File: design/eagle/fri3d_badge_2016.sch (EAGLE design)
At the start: 43 parts, among them K1 65100516121, Q1 MOSFET-NCHANNEL2N7002PW, U1 MCP73831

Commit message: fixed RGB LED footprint (+draft silk)
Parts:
- removed D2: (no value), SparkFun-LED:0.13_RGB_LEDPLCC
- added U$4: DRAGAN-PERSONAL_AVAGO-RGB-LED, Badge_EZR_V1:DRAGAN-PERSONAL_AVAGO-RGB-LED
- LED1: value (none) -> IR LED 1
- LED2: value (none) -> IR LED 2
- LED3: value (none) -> IR LED 3
- LED4: value (none) -> IR LED 4
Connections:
- removed net N$21: D2.RED, R9.2
- new net N$18: R9.2, U$4.P$4
- net N$19: now also R8.2, U$4.P$3; no longer D2.BLUE, R7.2
- net N$20: now also R7.2, U$4.P$2; no longer D2.GREEN, R8.2
- net VCC: now also U$4.P$1; no longer D2.ANODE
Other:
- moved on the sheet: R16, R17, R7, R8, R9
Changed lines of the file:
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@@
 <part name="GND8" library="SparkFun-Aesthetics" deviceset="GND" device=""/>
 <part name="S1" library="SparkFun-Electromechanical" deviceset="SWITCH-MOMENTARY-2" device="PTH"/>
-<part name="D2" library="SparkFun-LED" deviceset="0.13_RGB_LED" device="PLCC"/>
 <part name="ICSP" library="SparkFun-Connectors" deviceset="PINHD-2X3" device=""/>
 <part name="GND9" library="SparkFun-Aesthetics" deviceset="GND" device=""/>
@@
 <part name="R16" library="SparkFun-Passives" deviceset="RESISTOR" device="0805-RES" value="220"/>
 <part name="R17" library="SparkFun-Passives" deviceset="RESISTOR" device="0805-RES" value="220"/>
-<part name="LED1" library="led" deviceset="LED" device="CHIPLED_0805"/>
-<part name="LED2" library="led" deviceset="LED" device="CHIPLED_0805"/>
-<part name="LED3" library="led" deviceset="LED" device="CHIPLED_0805"/>
-<part name="LED4" library="led" deviceset="LED" device="CHIPLED_0805"/>
+<part name="LED1" library="led" deviceset="LED" device="CHIPLED_0805" value="IR LED 1"/>
+<part name="LED2" library="led" deviceset="LED" device="CHIPLED_0805" value="IR LED 2"/>
+<part name="LED3" library="led" deviceset="LED" device="CHIPLED_0805" value="IR LED 3"/>
+<part name="LED4" library="led" deviceset="LED" device="CHIPLED_0805" value="IR LED 4"/>
 <part name="Q2" library="crystal" deviceset="CRYSTAL" device="HC49S"/>
 <part name="J3" library="SparkFun-Connectors" deviceset="M02" device="JST-PTH-VERT"/>
@@
 <part name="GND10" library="SparkFun-Aesthetics" deviceset="GND" device=""/>
 <part name="S2" library="SparkFun-Electromechanical" deviceset="SWITCH-SPDT" device="-SMD-A"/>
+<part name="U$4" library="Badge_EZR_V1" deviceset="DRAGAN-PERSONAL_AVAGO-RGB-LED" device=""/>
 </parts>
 <sheets>
@@
 <instance part="GND8" gate="1" x="45.72" y="96.52" rot="R270"/>
 <instance part="S1" gate="G$1" x="185.42" y="160.02" rot="R180"/>
-<instance part="D2" gate="G$1" x="198.12" y="116.84" rot="R270"/>
 <instance part="ICSP" gate="A" x="-17.78" y="35.56"/>
 <instance part="GND9" gate="1" x="152.4" y="60.96"/>
 <instance part="SUPPLY4" gate="G$1" x="213.36" y="73.66"/>
 <instance part="SUPPLY5" gate="G$1" x="215.9" y="160.02"/>
-<instance part="R7" gate="G$1" x="182.88" y="124.46"/>
-<instance part="R8" gate="G$1" x="182.88" y="116.84"/>
-<instance part="SUPPLY6" gate="G$1" x="208.28" y="129.54"/>
+<instance part="R7" gate="G$1" x="182.88" y="104.14"/>
+<instance part="R8" gate="G$1" x="182.88" y="114.3"/>
+<instance part="SUPPLY6" gate="G$1" x="220.98" y="127"/>
 <instance part="GND17" gate="1" x="104.14" y="20.32"/>
 <instance part="U$3" gate="G$1" x="71.12" y="27.94"/>
@@
 <instance part="R6" gate="G$1" x="86.36" y="33.02"/>
 <instance part="R11" gate="G$1" x="86.36" y="43.18"/>
-<instance part="R9" gate="G$1" x="187.96" y="104.14" rot="R90"/>
-<instance part="R16" gate="G$1" x="182.88" y="99.06"/>
-<instance part="R17" gate="G$1" x="177.8" y="104.14" rot="R270"/>
+<instance part="R9" gate="G$1" x="187.96" y="129.54" rot="R270"/>
+<instance part="R16" gate="G$1" x="182.88" y="134.62"/>
+<instance part="R17" gate="G$1" x="177.8" y="129.54" rot="R90"/>
 <instance part="LED1" gate="G$1" x="205.74" y="71.12" rot="R270"/>
 <instance part="LED2" gate="G$1" x="205.74" y="55.88" rot="R270"/>
@@
 <instance part="GND10" gate="1" x="167.64" y="139.7"/>
 <instance part="S2" gate="1" x="-7.62" y="66.04"/>
+<instance part="U$4" gate="G$1" x="213.36" y="114.3" rot="R180"/>
 </instances>
 <busses>
@@
 </segment>
 <segment>
-<pinref part="D2" gate="G$1" pin="ANODE"/>
-<pinref part="SUPPLY6" gate="G$1" pin="VCC"/>
-<wire x1="208.28" y1="129.54" x2="208.28" y2="121.92" width="0.1524" layer="91"/>
-<wire x1="208.28" y1="121.92" x2="203.2" y2="121.92" width="0.1524" layer="91"/>
-</segment>
-<segment>
 <pinref part="SUPPLY7" gate="G$1" pin="VCC"/>
 <wire x1="104.14" y1="33.02" x2="99.06" y2="33.02" width="0.1524" layer="91"/>
@@
 <pinref part="S2" gate="1" pin="S"/>
 <wire x1="-2.54" y1="63.5" x2="7.62" y2="63.5" width="0.1524" layer="91"/>
+</segment>
+<segment>
+<pinref part="U$4" gate="G$1" pin="P$1"/>
+<pinref part="SUPPLY6" gate="G$1" pin="VCC"/>
+<wire x1="218.44" y1="114.3" x2="220.98" y2="114.3" width="0.1524" layer="91"/>
+<wire x1="220.98" y1="114.3" x2="220.98" y2="127" width="0.1524" layer="91"/>
 </segment>
 </net>
@@
 </segment>
 </net>
-<net name="N$19" class="0">
-<segment>
-<pinref part="R7" gate="G$1" pin="2"/>
-<pinref part="D2" gate="G$1" pin="BLUE"/>
-<wire x1="187.96" y1="124.46" x2="187.96" y2="121.92" width="0.1524" layer="91"/>
-<wire x1="187.96" y1="121.92" x2="195.58" y2="121.92" width="0.1524" layer="91"/>
-</segment>
-</net>
-<net name="N$21" class="0">
-<segment>
-<pinref part="D2" gate="G$1" pin="RED"/>
-<wire x1="187.96" y1="111.76" x2="195.58" y2="111.76" width="0.1524" layer="91"/>
-<pinref part="R9" gate="G$1" pin="2"/>
-<wire x1="187.96" y1="109.22" x2="187.96" y2="111.76" width="0.1524" layer="91"/>
-</segment>
-</net>
 <net name="RGB_BLUE" class="0">
 <segment>
 <pinref part="R7" gate="G$1" pin="1"/>
-<wire x1="177.8" y1="124.46" x2="160.02" y2="124.46" width="0.1524" layer="91"/>
-<label x="160.02" y="124.46" size="1.778" layer="95"/>
+<wire x1="177.8" y1="104.14" x2="160.02" y2="104.14" width="0.1524" layer="91"/>
+<label x="160.02" y="104.14" size="1.778" layer="95"/>
 </segment>
 <segment>
@@
 <segment>
 <pinref part="R8" gate="G$1" pin="1"/>
-<wire x1="177.8" y1="116.84" x2="160.02" y2="116.84" width="0.1524" layer="91"/>
-<label x="160.02" y="116.84" size="1.778" layer="95"/>
+<wire x1="177.8" y1="114.3" x2="160.02" y2="114.3" width="0.1524" layer="91"/>
+<label x="160.02" y="114.3" size="1.778" layer="95"/>
 </segment>
 <segment>
@@
 <net name="RGB_RED" class="0">
 <segment>
-<wire x1="177.8" y1="109.22" x2="160.02" y2="109.22" width="0.1524" layer="91"/>
-<label x="160.02" y="109.22" size="1.778" layer="95"/>
+<wire x1="177.8" y1="124.46" x2="160.02" y2="124.46" width="0.1524" layer="91"/>
+<label x="160.02" y="124.46" size="1.778" layer="95"/>
 <pinref part="R17" gate="G$1" pin="1"/>
 </segment>
@@
 <wire x1="106.68" y1="109.22" x2="142.24" y2="109.22" width="0.1524" layer="91"/>
 <label x="132.08" y="109.22" size="1.778" layer="95"/>
-</segment>
-</net>
-<net name="N$20" class="0">
-<segment>
-<pinref part="R8" gate="G$1" pin="2"/>
-<pinref part="D2" gate="G$1" pin="GREEN"/>
-<wire x1="187.96" y1="116.84" x2="195.58" y2="116.84" width="0.1524" layer="91"/>
 </segment>
 </net>
@@
 </segment>
 </net>
+<net name="N$19" class="0">
+<segment>
+<pinref part="R8" gate="G$1" pin="2"/>
+<pinref part="U$4" gate="G$1" pin="P$3"/>
+<wire x1="187.96" y1="114.3" x2="193.04" y2="114.3" width="0.1524" layer="91"/>
+</segment>
+</net>
+<net name="N$18" class="0">
+<segment>
+<pinref part="R9" gate="G$1" pin="2"/>
+<pinref part="U$4" gate="G$1" pin="P$4"/>
+<wire x1="187.96" y1="124.46" x2="193.04" y2="124.46" width="0.1524" layer="91"/>
+</segment>
+</net>
+<net name="N$20" class="0">
+<segment>
+<pinref part="R7" gate="G$1" pin="2"/>
+<pinref part="U$4" gate="G$1" pin="P$2"/>
+<wire x1="187.96" y1="104.14" x2="193.04" y2="104.14" width="0.1524" layer="91"/>
+</segment>
+</net>

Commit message: fixed USB connector (Mouser)
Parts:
- removed K1: 65100516121, Input-Output_Connectors_rev15d:65100516121
- added U$5: OCTA-CORE_MCIRO-USB2MOUSER, OCTA-EZR_v1:OCTA-CORE_MCIRO-USB2MOUSER
- LED5: value (none) -> LED
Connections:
- net GND: now also U$5.P$5, U$5.P$6, U$5.P$7; no longer K1.5GND, K1.GND@1, K1.GND@2
- net N$1: now also U$5.P$2; no longer K1.2D-
- net N$2: now also U$5.P$3; no longer K1.3D+
- net USBVCC: now also U$5.P$1; no longer K1.1VCC
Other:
- moved on the sheet: R1, R2
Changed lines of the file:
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@@
 <part name="SUPPLY8" library="SparkFun-Aesthetics" deviceset="VCC" device=""/>
 <part name="GND18" library="SparkFun-Aesthetics" deviceset="GND" device=""/>
-<part name="LED5" library="adafruit" deviceset="LED" device="CHIPLED_0805"/>
+<part name="LED5" library="adafruit" deviceset="LED" device="CHIPLED_0805" value="LED"/>
 <part name="R10" library="SparkFun-Passives" deviceset="RESISTOR" device="0805-RES" value="220"/>
 <part name="C7" library="SparkFun-Capacitors" deviceset="CAP" device="0805" value="0.1uF"/>
@@
 <part name="Q2" library="crystal" deviceset="CRYSTAL" device="HC49S"/>
 <part name="J3" library="SparkFun-Connectors" deviceset="M02" device="JST-PTH-VERT"/>
-<part name="K1" library="Input-Output_Connectors_rev15d" deviceset="65100516121" device=""/>
 <part name="U$2" library="GeekAmmo" deviceset="HEADER-06X1?" device="-MALE"/>
 <part name="R18" library="SparkFun-Passives" deviceset="RESISTOR" device="0805-RES" value="10K"/>
@@
 <part name="S2" library="SparkFun-Electromechanical" deviceset="SWITCH-SPDT" device="-SMD-A"/>
 <part name="U$4" library="Badge_EZR_V1" deviceset="DRAGAN-PERSONAL_AVAGO-RGB-LED" device=""/>
+<part name="U$5" library="OCTA-EZR_v1" deviceset="OCTA-CORE_MCIRO-USB2" device="" technology="MOUSER"/>
 </parts>
 <sheets>
@@
 <instance part="FRAME2" gate="G$1" x="-45.72" y="-7.62"/>
 <instance part="U$1" gate="G$1" x="88.9" y="109.22"/>
-<instance part="R1" gate="G$1" x="7.62" y="139.7"/>
-<instance part="R2" gate="G$1" x="7.62" y="132.08"/>
+<instance part="R1" gate="G$1" x="7.62" y="137.16"/>
+<instance part="R2" gate="G$1" x="7.62" y="129.54"/>
 <instance part="GND1" gate="1" x="-7.62" y="142.24"/>
 <instance part="U1" gate="G$1" x="0" y="96.52"/>
@@
 <instance part="Q2" gate="G$1" x="63.5" y="96.52" rot="R90"/>
 <instance part="J3" gate="G$1" x="-30.48" y="63.5"/>
-<instance part="K1" gate="G$1" x="-22.86" y="134.62" rot="R180"/>
 <instance part="U$2" gate="G$1" x="20.32" y="35.56"/>
 <instance part="R18" gate="G$1" x="167.64" y="147.32" rot="R270"/>
@@
 <instance part="S2" gate="1" x="-7.62" y="66.04"/>
 <instance part="U$4" gate="G$1" x="213.36" y="114.3" rot="R180"/>
+<instance part="U$5" gate="G$1" x="-25.4" y="137.16" rot="R180"/>
 </instances>
 <busses>
@@
 </segment>
 <segment>
-<pinref part="K1" gate="G$1" pin="5GND"/>
-<wire x1="-15.24" y1="139.7" x2="-15.24" y2="144.78" width="0.1524" layer="91"/>
 <wire x1="-15.24" y1="144.78" x2="-15.24" y2="147.32" width="0.1524" layer="91"/>
 <wire x1="-15.24" y1="147.32" x2="-7.62" y2="147.32" width="0.1524" layer="91"/>
 <pinref part="GND1" gate="1" pin="GND"/>
 <wire x1="-7.62" y1="147.32" x2="-7.62" y2="144.78" width="0.1524" layer="91"/>
-<pinref part="K1" gate="G$1" pin="GND@1"/>
-<wire x1="-17.78" y1="144.78" x2="-15.24" y2="144.78" width="0.1524" layer="91"/>
+<junction x="-15.24" y="147.32"/>
+<pinref part="U$5" gate="G$1" pin="P$7"/>
+<wire x1="-22.86" y1="147.32" x2="-15.24" y2="147.32" width="0.1524" layer="91"/>
+<pinref part="U$5" gate="G$1" pin="P$6"/>
+<wire x1="-22.86" y1="144.78" x2="-15.24" y2="144.78" width="0.1524" layer="91"/>
+<pinref part="U$5" gate="G$1" pin="P$5"/>
+<wire x1="-20.32" y1="134.62" x2="-15.24" y2="134.62" width="0.1524" layer="91"/>
+<wire x1="-15.24" y1="134.62" x2="-15.24" y2="144.78" width="0.1524" layer="91"/>
 <junction x="-15.24" y="144.78"/>
-<pinref part="K1" gate="G$1" pin="GND@2"/>
-<wire x1="-17.78" y1="147.32" x2="-15.24" y2="147.32" width="0.1524" layer="91"/>
-<junction x="-15.24" y="147.32"/>
 </segment>
 <segment>
@@
 <segment>
 <pinref part="R1" gate="G$1" pin="2"/>
-<wire x1="12.7" y1="139.7" x2="20.32" y2="139.7" width="0.1524" layer="91"/>
-<label x="17.78" y="139.7" size="1.778" layer="95"/>
+<wire x1="12.7" y1="137.16" x2="20.32" y2="137.16" width="0.1524" layer="91"/>
+<label x="17.78" y="137.16" size="1.778" layer="95"/>
 </segment>
 <segment>
@@
 <segment>
 <pinref part="R2" gate="G$1" pin="2"/>
-<wire x1="12.7" y1="132.08" x2="20.32" y2="132.08" width="0.1524" layer="91"/>
-<label x="17.78" y="132.08" size="1.778" layer="95"/>
+<wire x1="12.7" y1="129.54" x2="20.32" y2="129.54" width="0.1524" layer="91"/>
+<label x="17.78" y="129.54" size="1.778" layer="95"/>
 </segment>
 <segment>
@@
 </segment>
 <segment>
-<wire x1="0" y1="124.46" x2="20.32" y2="124.46" width="0.1524" layer="91"/>
 <label x="10.16" y="124.46" size="1.778" layer="95"/>
-<wire x1="0" y1="124.46" x2="0" y2="129.54" width="0.1524" layer="91"/>
-<pinref part="K1" gate="G$1" pin="1VCC"/>
-<wire x1="-15.24" y1="129.54" x2="0" y2="129.54" width="0.1524" layer="91"/>
+<pinref part="U$5" gate="G$1" pin="P$1"/>
+<wire x1="-20.32" y1="124.46" x2="20.32" y2="124.46" width="0.1524" layer="91"/>
 </segment>
 </net>
@@
 </segment>
 </net>
-<net name="N$1" class="0">
-<segment>
-<pinref part="R2" gate="G$1" pin="1"/>
-<pinref part="K1" gate="G$1" pin="2D-"/>
-<wire x1="2.54" y1="132.08" x2="-15.24" y2="132.08" width="0.1524" layer="91"/>
-</segment>
-</net>
-<net name="N$2" class="0">
-<segment>
-<pinref part="R1" gate="G$1" pin="1"/>
-<wire x1="2.54" y1="139.7" x2="0" y2="139.7" width="0.1524" layer="91"/>
-<wire x1="0" y1="139.7" x2="0" y2="134.62" width="0.1524" layer="91"/>
-<pinref part="K1" gate="G$1" pin="3D+"/>
-<wire x1="0" y1="134.62" x2="-15.24" y2="134.62" width="0.1524" layer="91"/>
-</segment>
-</net>
 <net name="A0" class="0">
 <segment>
@@
 </segment>
 </net>
+<net name="N$1" class="0">
+<segment>
+<pinref part="R2" gate="G$1" pin="1"/>
+<wire x1="2.54" y1="129.54" x2="0" y2="129.54" width="0.1524" layer="91"/>
+<wire x1="0" y1="129.54" x2="0" y2="127" width="0.1524" layer="91"/>
+<pinref part="U$5" gate="G$1" pin="P$2"/>
+<wire x1="0" y1="127" x2="-20.32" y2="127" width="0.1524" layer="91"/>
+</segment>
+</net>
+<net name="N$2" class="0">
+<segment>
+<pinref part="R1" gate="G$1" pin="1"/>
+<wire x1="2.54" y1="137.16" x2="-2.54" y2="137.16" width="0.1524" layer="91"/>
+<wire x1="-2.54" y1="137.16" x2="-2.54" y2="129.54" width="0.1524" layer="91"/>
+<pinref part="U$5" gate="G$1" pin="P$3"/>
+<wire x1="-2.54" y1="129.54" x2="-20.32" y2="129.54" width="0.1524" layer="91"/>
+</segment>
+</net>

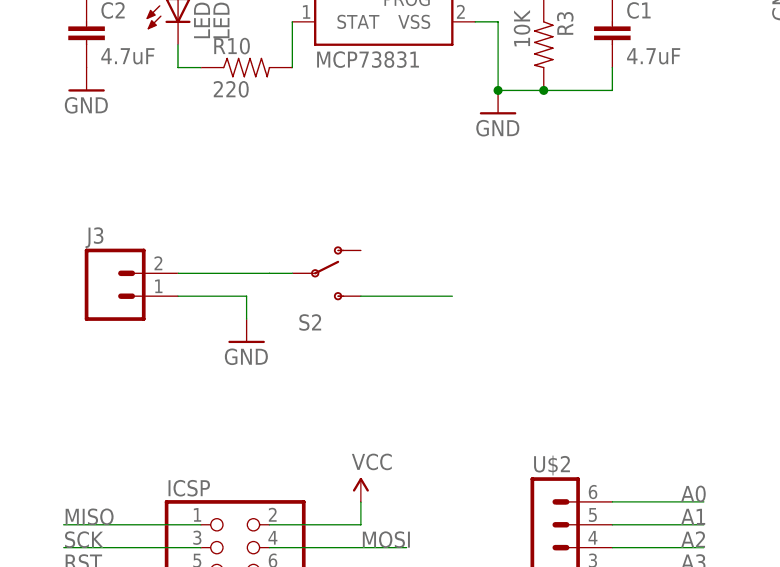
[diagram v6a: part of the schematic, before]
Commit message: fixed switch footprint
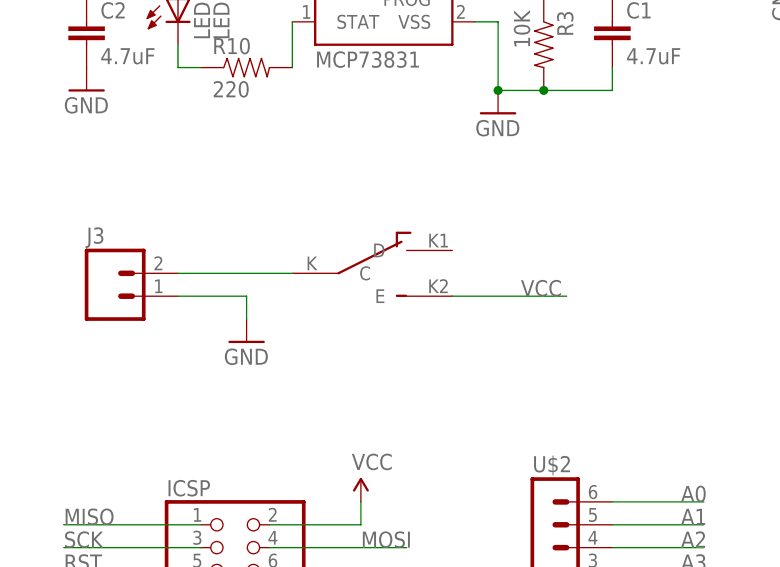
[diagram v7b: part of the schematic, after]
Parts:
- removed S2: (no value), SparkFun-Electromechanical:SWITCH-SPDT-SMD-A
- added U$6: SLIDE-SWITCH, FriedCamp:SLIDE-SWITCH
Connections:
- net N$17: now also U$6.C; no longer S2.P
- net VCC: now also U$6.E; no longer S2.S
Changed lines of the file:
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@@
 <part name="R18" library="SparkFun-Passives" deviceset="RESISTOR" device="0805-RES" value="10K"/>
 <part name="GND10" library="SparkFun-Aesthetics" deviceset="GND" device=""/>
-<part name="S2" library="SparkFun-Electromechanical" deviceset="SWITCH-SPDT" device="-SMD-A"/>
 <part name="U$4" library="Badge_EZR_V1" deviceset="DRAGAN-PERSONAL_AVAGO-RGB-LED" device=""/>
 <part name="U$5" library="OCTA-EZR_v1" deviceset="OCTA-CORE_MCIRO-USB2" device="" technology="MOUSER"/>
+<part name="U$6" library="FriedCamp" deviceset="SLIDE-SWITCH" device=""/>
 </parts>
 <sheets>
@@
 <instance part="R18" gate="G$1" x="167.64" y="147.32" rot="R270"/>
 <instance part="GND10" gate="1" x="167.64" y="139.7"/>
-<instance part="S2" gate="1" x="-7.62" y="66.04"/>
 <instance part="U$4" gate="G$1" x="213.36" y="114.3" rot="R180"/>
 <instance part="U$5" gate="G$1" x="-25.4" y="137.16" rot="R180"/>
+<instance part="U$6" gate="G$1" x="-2.54" y="66.04"/>
 </instances>
 <busses>
@@
 </segment>
 <segment>
-<pinref part="S2" gate="1" pin="S"/>
-<wire x1="-2.54" y1="63.5" x2="7.62" y2="63.5" width="0.1524" layer="91"/>
+<label x="15.24" y="63.5" size="1.778" layer="95"/>
+<pinref part="U$6" gate="G$1" pin="E"/>
+<wire x1="7.62" y1="63.5" x2="20.32" y2="63.5" width="0.1524" layer="91"/>
 </segment>
 <segment>
@@
 </segment>
 </net>
-<net name="N$17" class="0">
-<segment>
-<pinref part="J3" gate="G$1" pin="2"/>
-<pinref part="S2" gate="1" pin="P"/>
-<wire x1="-22.86" y1="66.04" x2="-12.7" y2="66.04" width="0.1524" layer="91"/>
-<wire x1="-12.7" y1="66.04" x2="-10.16" y2="66.04" width="0.1524" layer="91"/>
-</segment>
-</net>
 <net name="N$19" class="0">
 <segment>
@@
 </segment>
 </net>
+<net name="N$17" class="0">
+<segment>
+<pinref part="J3" gate="G$1" pin="2"/>
+<pinref part="U$6" gate="G$1" pin="C"/>
+<wire x1="-22.86" y1="66.04" x2="-10.16" y2="66.04" width="0.1524" layer="91"/>
+</segment>
+</net>

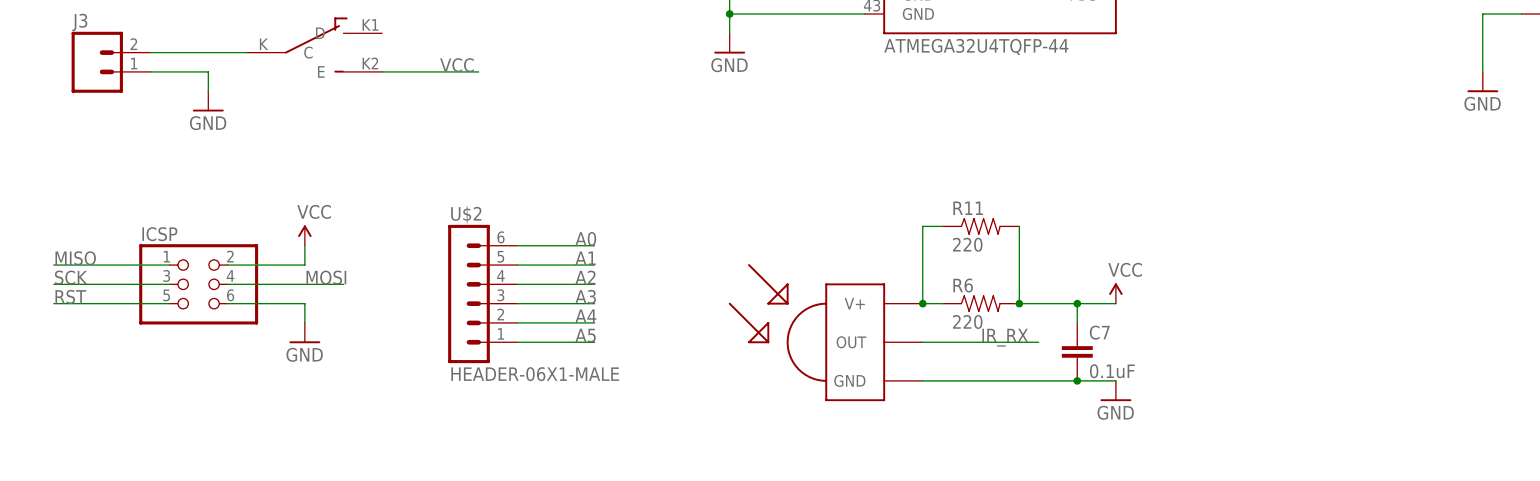
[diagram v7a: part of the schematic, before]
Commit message: replaced ICSP header with Tag Connect pads
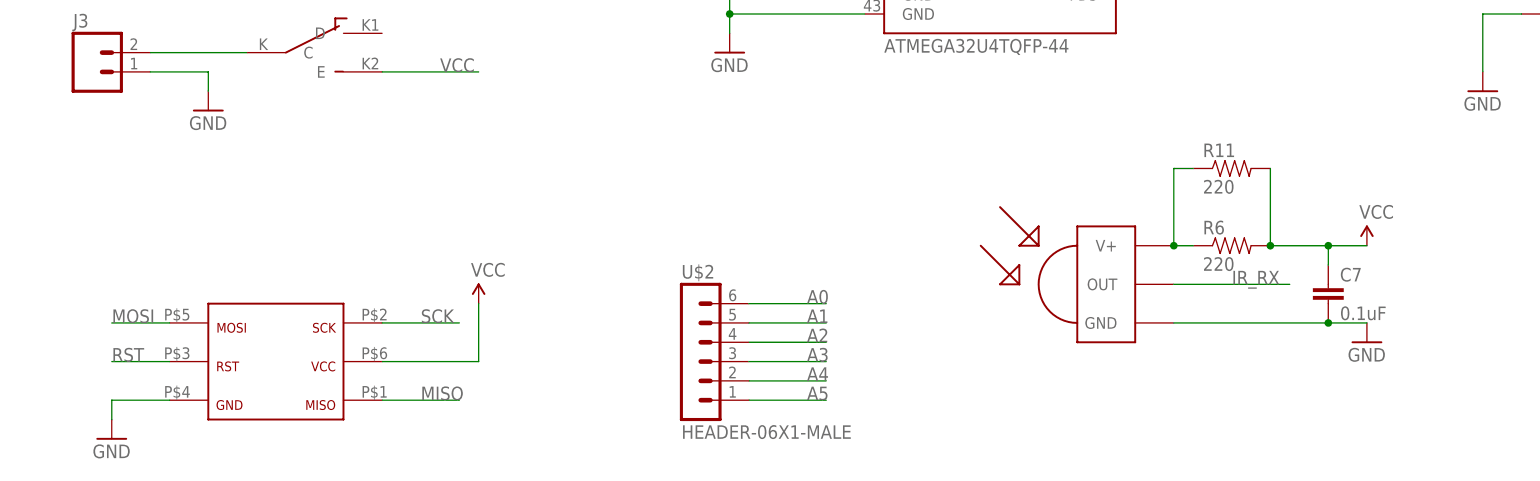
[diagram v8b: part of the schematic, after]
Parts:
- removed ICSP: (no value), SparkFun-Connectors:PINHD-2X3
- added U$7: OCTA-CORE_TC2030-IDC, Badge_EZR_V1:OCTA-CORE_TC2030-IDC
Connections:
- net GND: now also U$7.P$6; no longer ICSP.6
- net MISO: now also U$7.P$1; no longer ICSP.1
- net MOSI: now also U$7.P$4; no longer ICSP.4
- net RST: now also U$7.P$5; no longer ICSP.5
- net SCK: now also U$7.P$3; no longer ICSP.3
- net VCC: now also U$7.P$2; no longer ICSP.2
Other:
- moved on the sheet: C7, R11, R6, U$2
